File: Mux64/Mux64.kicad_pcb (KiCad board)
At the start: 4 copper layers, 201.3 x 130.3 mm, 125 parts, among them J1 QTE-020-01-X-D-A, J10 Conn_01x24, J11 Screw_Terminal_01x12, J12 Screw_Terminal_01x06, J13 Screw_Terminal_01x12, J14 Screw_Terminal_01x12, J16 Screw_Terminal_01x12, J17 Screw_Terminal_01x12, J18 Screw_Terminal_01x12, J2 QTE-020-01-X-D-A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

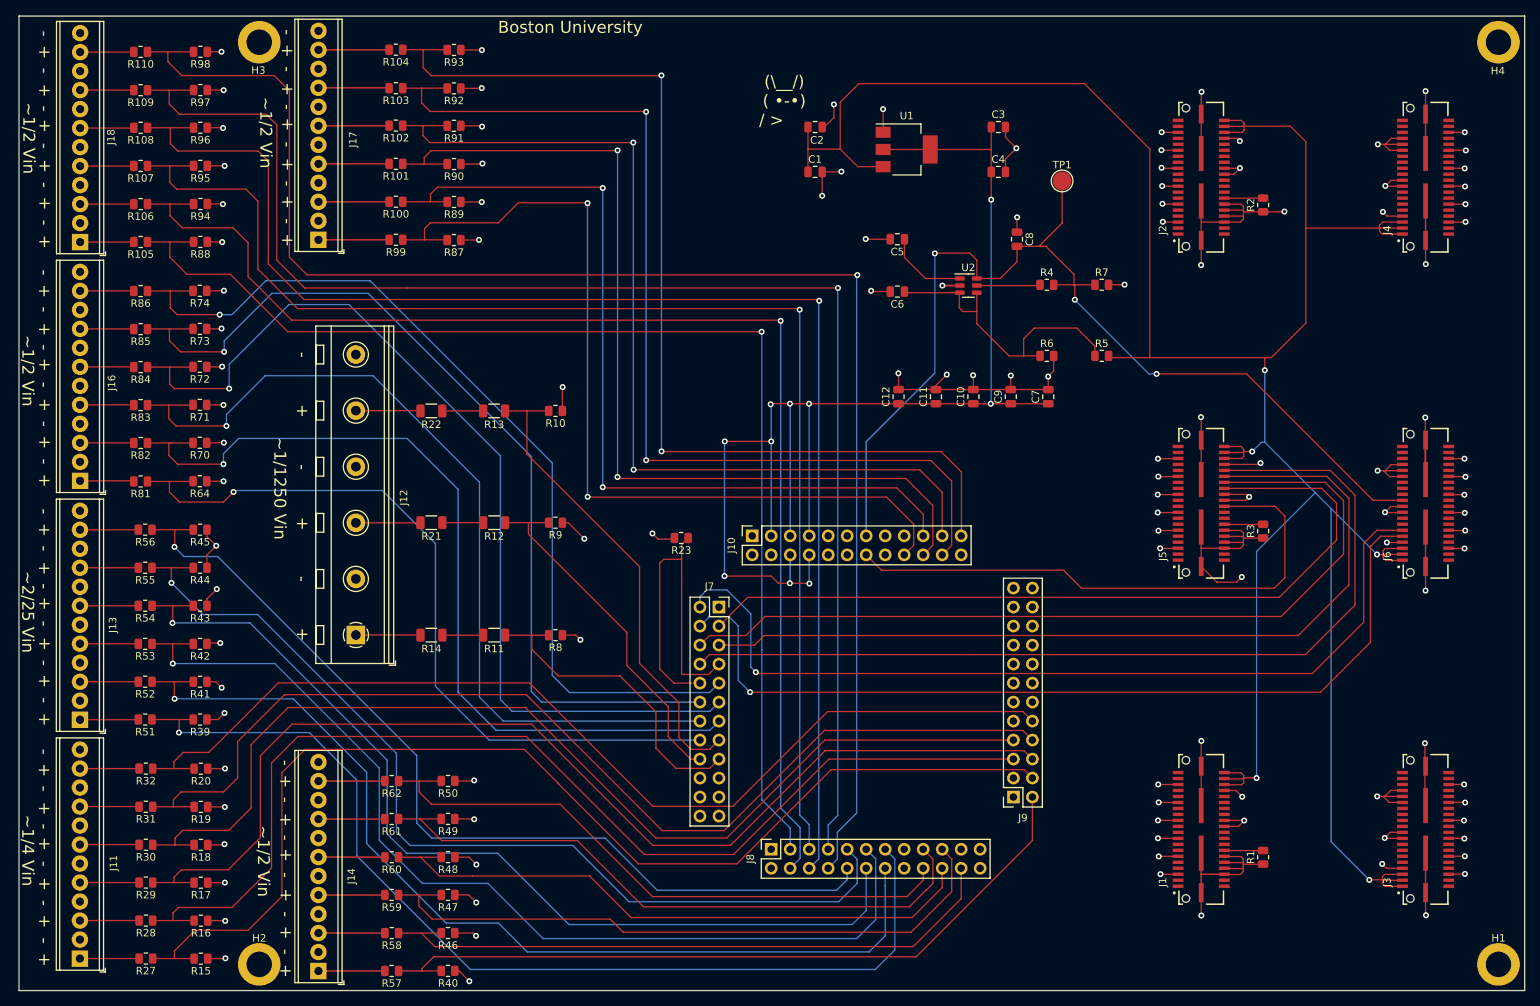
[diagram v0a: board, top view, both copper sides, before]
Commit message: Power and Ground traces resized
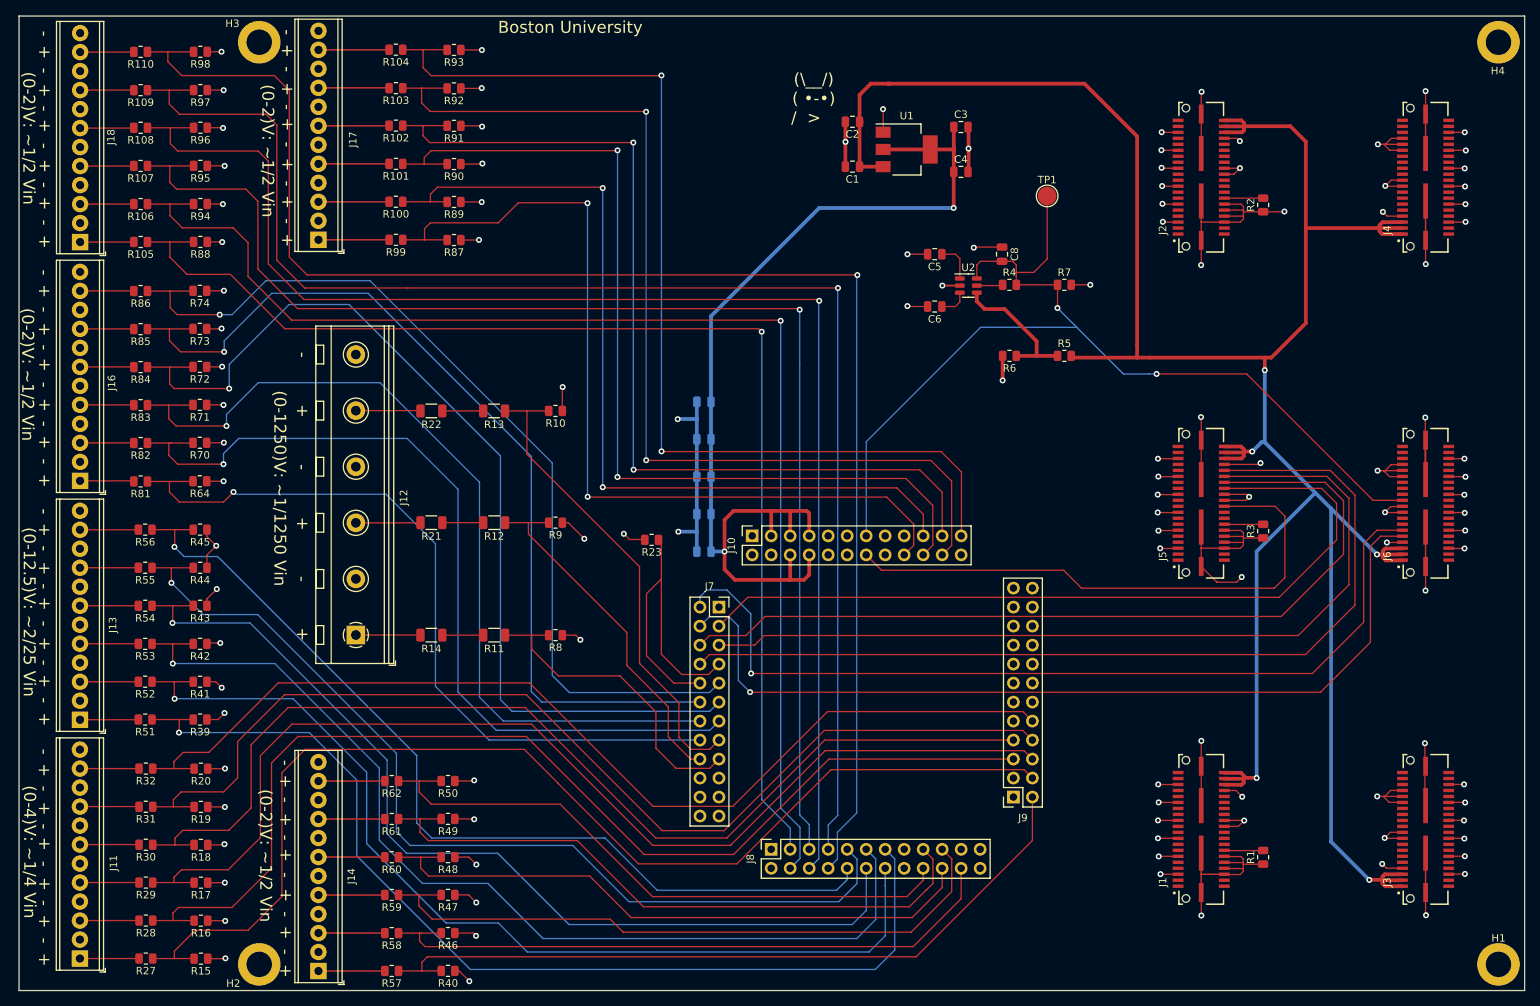
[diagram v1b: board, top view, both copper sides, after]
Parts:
- C10, C11, C12, C7, C9: moved to B.Cu
- moved C7 50.5 mm to (144.5, 96.5), turned to 180 degrees
- moved C9 43.9 mm to (144.5, 91.5), turned to 180 degrees
- moved C10 37.6 mm to (144.5, 86.5), turned to 180 degrees
- moved C11 31.5 mm to (144.5, 81.5), turned to 180 degrees
- moved C12 26.0 mm to (144.5, 76.5), turned to 180 degrees
- moved C5 5.39 mm to (175.3, 56.7)
- moved C6 5.39 mm to (175.3, 63.7)
- moved C1 5.05 mm to (164.3, 45.0), turned to 180 degrees
- moved C2 5.05 mm to (164.3, 39.0), turned to 180 degrees
- moved C3 5.00 mm to (178.8, 39.7)
- moved C4 5.00 mm to (178.8, 45.7)
- moved R4 5.00 mm to (185.3, 60.8)
- moved R5 5.00 mm to (192.7, 70.3)
- moved R6 5.00 mm to (185.3, 70.3), turned to 180 degrees
- moved R7 5.00 mm to (192.7, 60.8)
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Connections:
- net MUX64_A42 renamed MUX64_A11
- net Net-(J12-Pad1) renamed /mux64-regulators/screw-terminals/HV0
- net Net-(J12-Pad3) renamed /mux64-regulators/screw-terminals/HV1
- net Net-(J12-Pad5) renamed /mux64-regulators/screw-terminals/HV2
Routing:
- net 1.2V: track 185.3 -> 138.5 mm, vias 10 -> 2
- net Net-(C6-Pad1): track 41.1 -> 23.0 mm
- net LV_RB: track 358.9 -> 350.3 mm
- net MUX64_A11: track 494.1 -> 486.0 mm, vias 118 -> 114
- net Net-(C5-Pad1): track 11.0 -> 5.32 mm
- net B_a4: track 141.5 -> 135.9 mm, vias 3 -> 2
- net Net-(R4-Pad1): track 8.49 -> 3.49 mm
- net MUX64_A0: track 47.5 -> 44.6 mm
- net MUX64_A30: track 85.7 -> 86.7 mm
- net MUX64_A31: track 83.1 -> 83.9 mm
- net MUX64_A33: track 85.4 -> 86.3 mm
- net MUX64_A5: track 119.0 -> 118.2 mm
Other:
- board text added: "(0-12.5)V: ~2/25 Vin"
- board text added: "(0-1250)V: ~1/1250 Vin"
- board text added: "(0-2)V: ~1/2 Vin"
- board text added: "(0-4)V: ~1/4 Vin"
- board text removed: "~1/1250 Vin"
- board text removed: "~1/2 Vin"
- board text removed: "~1/4 Vin"
- board text removed: "~2/25 Vin"
